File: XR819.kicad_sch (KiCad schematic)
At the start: 25 parts, among them J1 Conn_01x06, J2 Conn_01x06, U1 XR819, U2 NC, Y1 Crystal_GND24_Small

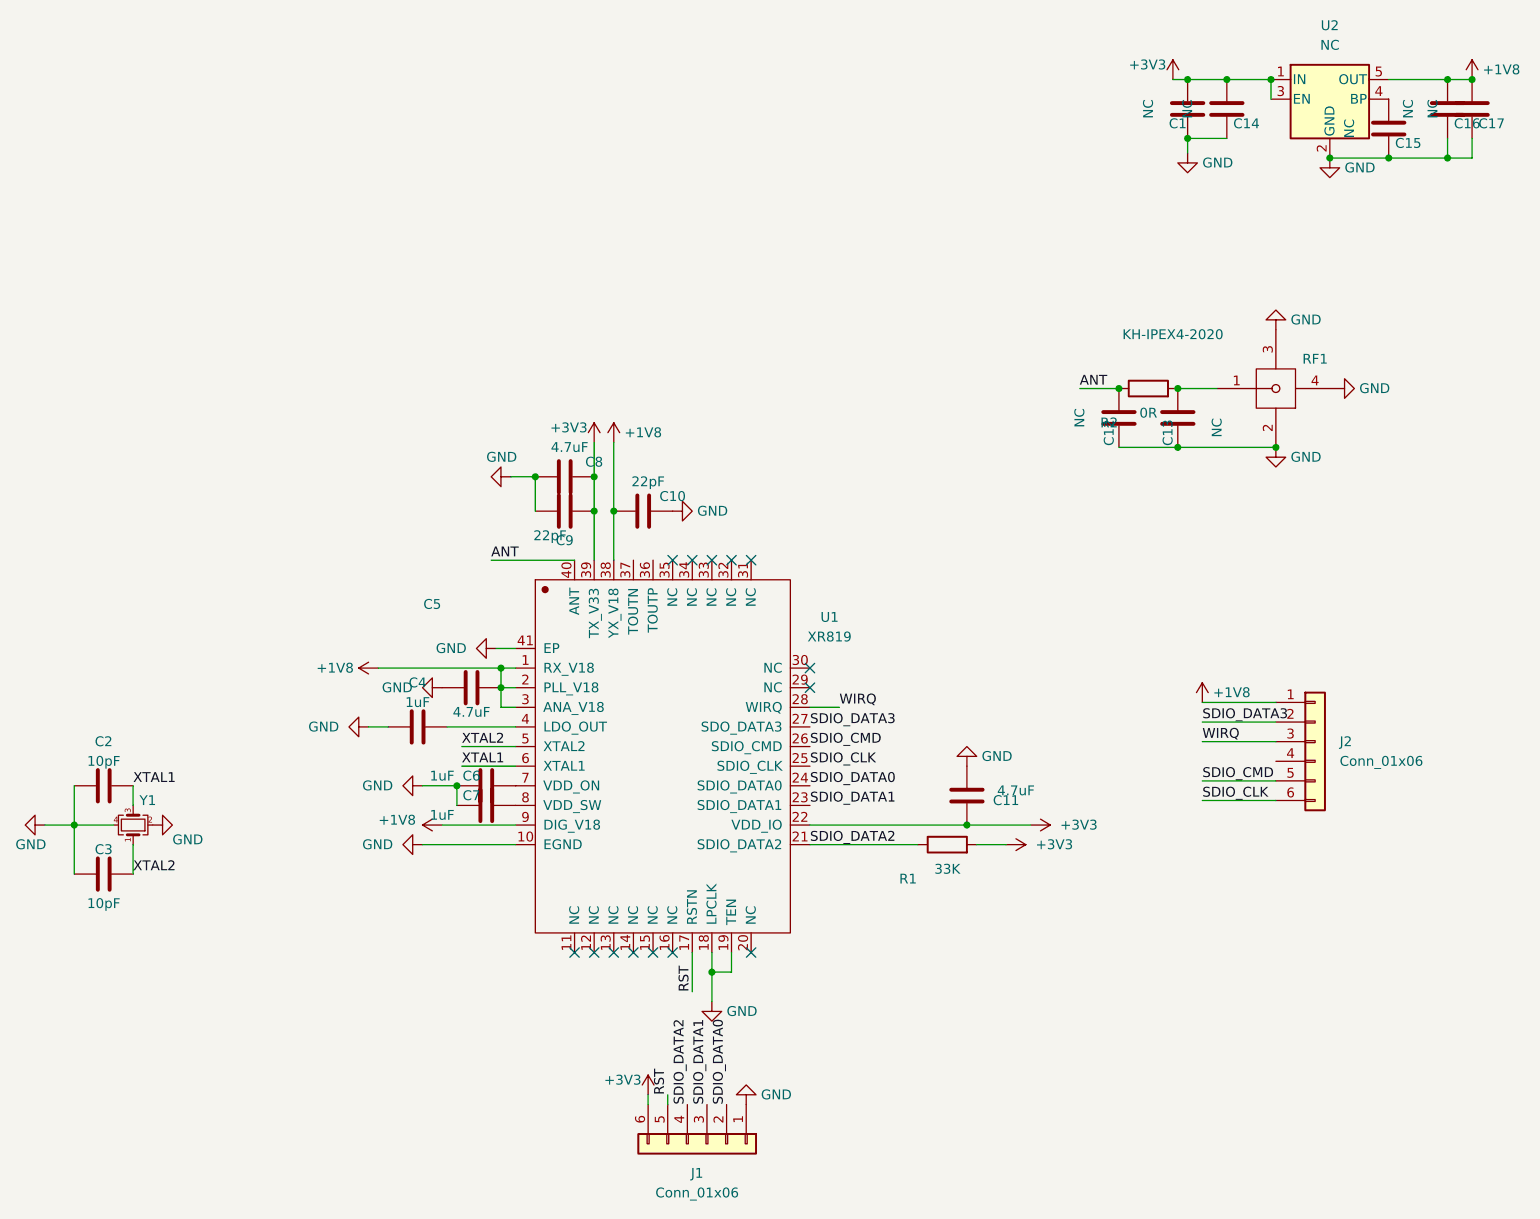
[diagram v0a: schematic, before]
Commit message: add comment on osc
Signed-off-by: ncerzzk <huangcmzzk@gmail.com>
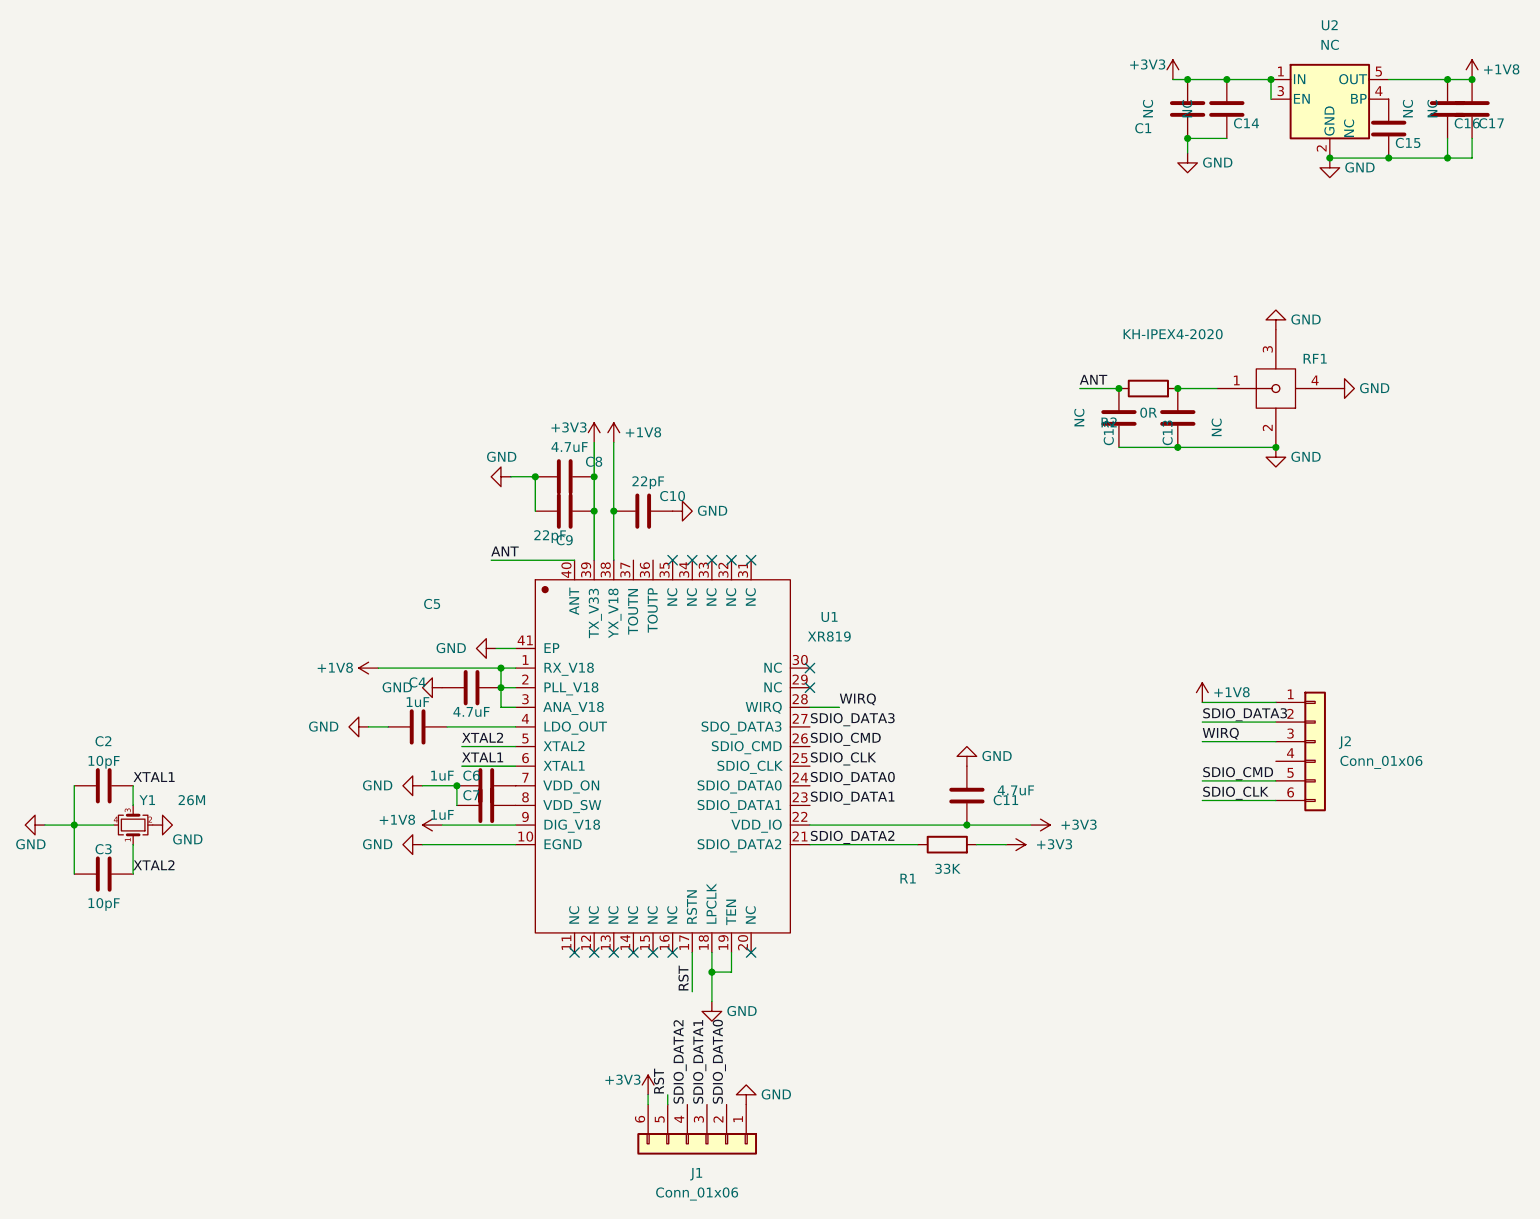
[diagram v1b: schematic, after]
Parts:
- Y1: value Crystal_GND24_Small -> 26M
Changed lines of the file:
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@@
     (in_bom yes) (on_board yes)
     (property "Reference" "Y1" (id 0) (at 65.405 114.3 90))
-    (property "Value" "Crystal_GND24_Small" (id 1) (at 67.945 118.11 0)
-      (effects (font (size 1.27 1.27)) hide)
-    )
+    (property "Value" "26M" (id 1) (at 71.12 114.3 90))
     (property "Footprint" "Crystal:Crystal_SMD_EuroQuartz_MT-4Pin_3.2x2.5mm" (id 2) (at 63.5 117.475 0)
       (effects (font (size 1.27 1.27)) hide)
@@
   (symbol (lib_id "Device:C") (at 200.025 24.765 180) (unit 1)
     (in_bom yes) (on_board yes)
-    (property "Reference" "C1" (id 0) (at 198.755 26.67 0))
+    (property "Reference" "C1" (id 0) (at 194.31 27.305 0))
     (property "Value" "NC" (id 1) (at 194.945 24.765 90))
     (property "Footprint" "Capacitor_SMD:C_0402_1005Metric" (id 2) (at 199.0598 20.955 0)
@@
     )
     (path "/56a4b58e-b3af-4945-a60c-e28e4c9e40e9"
-      (reference "Y1") (unit 1) (value "Crystal_GND24_Small") (footprint "Crystal:Crystal_SMD_EuroQuartz_MT-4Pin_3.2x2.5mm")
-    )
-  )
+      (reference "Y1") (unit 1) (value "26M") (footprint "Crystal:Crystal_SMD_EuroQuartz_MT-4Pin_3.2x2.5mm")
+    )
+  )
